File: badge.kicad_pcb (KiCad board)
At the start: 2 copper layers, 76.2 x 127 mm, 29 parts, among them J1 TC2030, SW1 SW_Push, SW2 SW_Push, SW3 SW_Push, SW4 SW_Push, SW5 SW_Push, U1 NHD-C12832A1Z-FSRGB-FBW-3V

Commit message: Add graffiti
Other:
- board text added: "Designed by SplitPixl, Assembled by you!"
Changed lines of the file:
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@@
 			(at 3.25 -2 0)
 			(layer "F.SilkS")
+			(hide yes)
 			(effects
 				(font
@@
 			(at 3.25 -2 0)
 			(layer "F.SilkS")
+			(hide yes)
 			(effects
 				(font
@@
 			(at 3.25 -2 0)
 			(layer "F.SilkS")
+			(hide yes)
 			(effects
 				(font
@@
 			(at 3.25 -2 0)
 			(layer "F.SilkS")
+			(hide yes)
 			(effects
 				(font
@@
 			(at 3.25 -2 0)
 			(layer "F.SilkS")
+			(hide yes)
 			(effects
 				(font
@@
 		)
 	)
+	(gr_text "Designed by SplitPixl,\nAssembled by you!"
+		(at 63.5 151.327 0)
+		(layer "B.SilkS")
+		(effects
+			(font
+				(size 1 1)
+				(thickness 0.1)
+			)
+			(justify bottom mirror)
+		)
+	)

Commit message: board can be turned off
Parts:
- added SW6: SW_SPST, FTbadge:SW_SLW-1277744-3A-N-D, F.Cu at (92.1, 42.1)
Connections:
- D1 pad 2: Net-(BT1-+) -> Net-(D1-A)
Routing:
- net Net-(D1-A): track 0.00 -> 54.7 mm
- net Net-(BT1-+): track 11.0 -> 39.3 mm

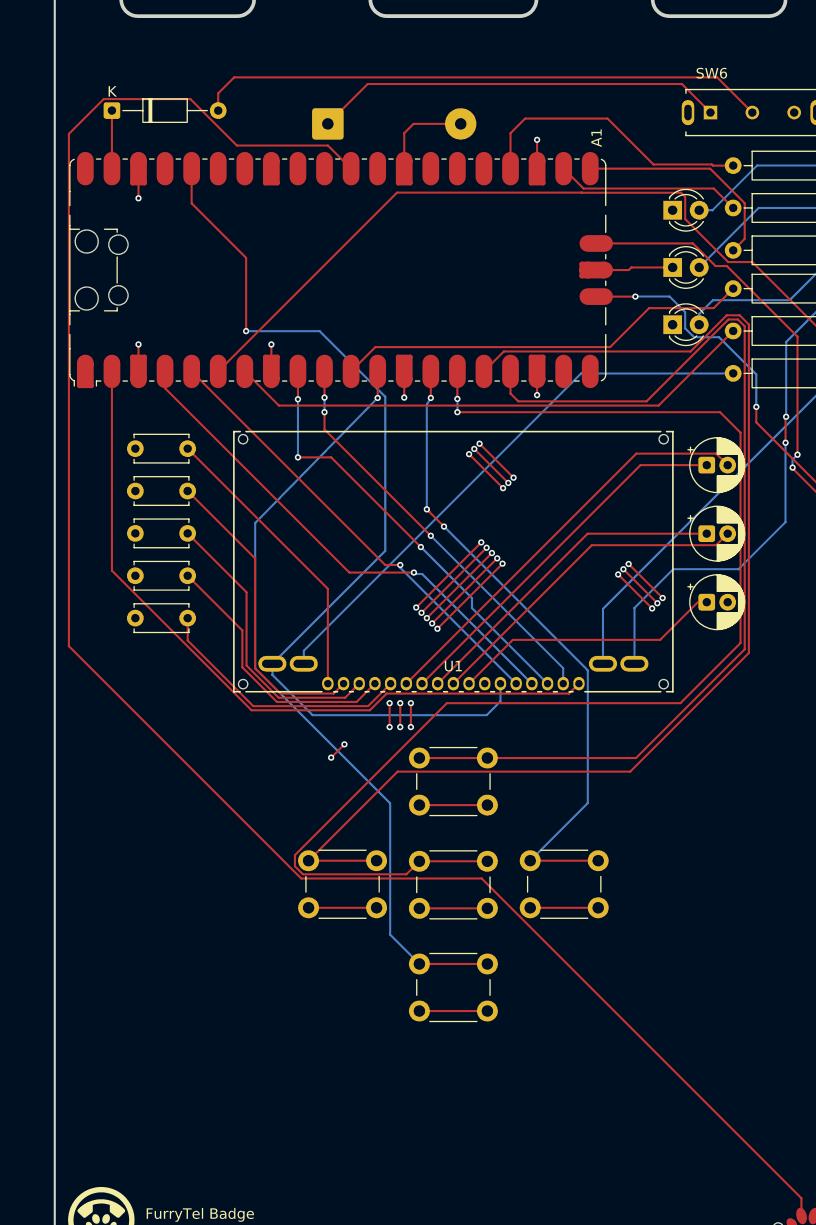
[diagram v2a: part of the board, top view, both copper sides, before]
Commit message: Add SAO connector
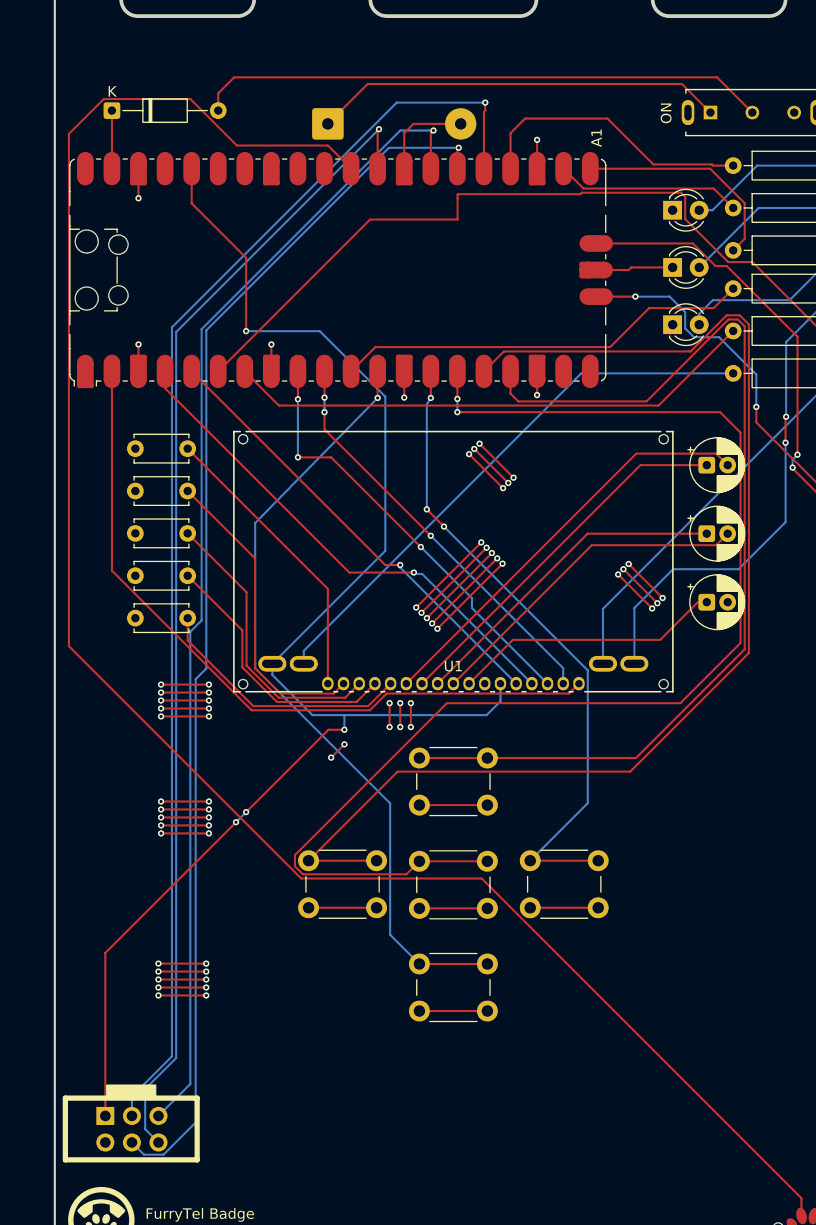
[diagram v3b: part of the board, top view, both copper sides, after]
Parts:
- added X1: Simple_Addon_v2, FTbadge:Simple_Addon_v2-BADGE-2x3, F.Cu at (32.7, 139.3)
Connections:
- A1 pad 25: unconnected-(A1-GPIO19-Pad25) -> Net-(A1-GPIO19)
- A1 pad 26: unconnected-(A1-GPIO20-Pad26) -> Net-(A1-GPIO20)
- A1 pad 27: unconnected-(A1-GPIO21-Pad27) -> Net-(A1-GPIO21)
- A1 pad 29: unconnected-(A1-GPIO22-Pad29) -> Net-(A1-GPIO22)
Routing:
- net Net-(A1-GPIO19): track 0.00 -> 122.2 mm, vias 0 -> 1
- net Net-(A1-GPIO20): track 0.00 -> 117.4 mm, vias 0 -> 1
- net Net-(A1-GPIO21): track 0.00 -> 110.7 mm, vias 0 -> 1
- net Net-(A1-GPIO22): track 0.00 -> 110.5 mm, vias 0 -> 1
- net (no net): track 0.00 -> 68.6 mm, vias 0 -> 30
- net +3V3: track 90.3 -> 138.9 mm, vias 1 -> 4
- net Net-(A1-GPIO4): track 76.2 -> 77.6 mm
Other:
- board text added: "ON"

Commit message: Add cat!
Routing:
- net GND: track 147.3 -> 215.9 mm, vias 37 -> 67
- net (no net): track 68.6 -> 0.00 mm, vias 30 -> 0

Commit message: mild cleanup
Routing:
- net Net-(A1-GPIO19): track 122.2 -> 125.8 mm
- net Net-(A1-GPIO21): track 110.7 -> 110.2 mm
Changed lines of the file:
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@@
 			(at 0 -5.5 0)
 			(layer "B.SilkS")
+			(hide yes)
 			(effects
 				(font
@@
 			(at 0 -8.509 0)
 			(layer "F.Fab")
+			(hide yes)
 			(effects
 				(font
@@
 	)
 	(segment
-		(start 63.881 47.46)
-		(end 63.881 45.593)
+		(start 63.881 45.593)
+		(end 63.881 47.46)
 		(width 0.2)
 		(layer "F.Cu")
@@
 	)
 	(segment
-		(start 63.881 45.593)
-		(end 64.008 45.466)
+		(start 62.23 44.704)
+		(end 62.992 44.704)
+		(width 0.2)
+		(layer "F.Cu")
+		(net "Net-(A1-GPIO20)")
+	)
+	(segment
+		(start 62.992 44.704)
+		(end 63.881 45.593)
 		(width 0.2)
 		(layer "F.Cu")
@@
 	)
 	(via
-		(at 64.008 45.466)
+		(at 62.23 44.704)
 		(size 0.6)
 		(drill 0.3)
@@
 	)
 	(segment
-		(start 39.883471 62.917215)
-		(end 39.883471 95.244529)
+		(start 33.9356 141.7083)
+		(end 32.772 140.5447)
 		(width 0.2)
 		(layer "B.Cu")
@@
 	)
 	(segment
-		(start 35.793979 141.7083)
-		(end 33.9356 141.7083)
+		(start 58.096686 44.704)
+		(end 39.883471 62.917215)
 		(width 0.2)
 		(layer "B.Cu")
@@
 	)
 	(segment
-		(start 39.883471 95.244529)
-		(end 38.862 96.266)
+		(start 35.793979 141.7083)
+		(end 33.9356 141.7083)
 		(width 0.2)
 		(layer "B.Cu")
@@
 	)
 	(segment
-		(start 38.862 96.266)
-		(end 38.862 138.640279)
+		(start 38.862 138.640279)
+		(end 35.793979 141.7083)
 		(width 0.2)
 		(layer "B.Cu")
@@
 	)
 	(segment
-		(start 57.334686 45.466)
-		(end 39.883471 62.917215)
+		(start 39.883471 95.244529)
+		(end 38.862 96.266)
 		(width 0.2)
 		(layer "B.Cu")
@@
 	)
 	(segment
-		(start 64.008 45.466)
-		(end 57.334686 45.466)
+		(start 38.862 96.266)
+		(end 38.862 138.640279)
 		(width 0.2)
 		(layer "B.Cu")
@@
 	)
 	(segment
-		(start 33.9356 141.7083)
-		(end 32.772 140.5447)
+		(start 39.883471 62.917215)
+		(end 39.883471 95.244529)
 		(width 0.2)
 		(layer "B.Cu")
@@
 	)
 	(segment
-		(start 38.862 138.640279)
-		(end 35.793979 141.7083)
+		(start 62.23 44.704)
+		(end 58.096686 44.704)
 		(width 0.2)
 		(layer "B.Cu")
@@
 	)
 	(segment
-		(start 61.595 43.815)
+		(start 60.198 43.815)
+		(end 61.087 43.815)
+		(width 0.2)
+		(layer "F.Cu")
+		(net "Net-(A1-GPIO21)")
+	)
+	(segment
+		(start 61.087 43.815)
 		(end 61.341 44.069)
 		(width 0.2)
@@
 	)
 	(via
-		(at 61.595 43.815)
+		(at 60.198 43.815)
 		(size 0.6)
 		(drill 0.3)
@@
 	)
 	(segment
-		(start 39.4335 90.646135)
-		(end 39.4335 62.8015)
+		(start 39.4335 62.8015)
+		(end 39.4335 90.646135)
 		(width 0.2)
 		(layer "B.Cu")
@@
 	)
 	(segment
-		(start 38.354 91.725635)
-		(end 39.4335 90.646135)
+		(start 38.354 134.9627)
+		(end 35.312 138.0047)
 		(width 0.2)
 		(layer "B.Cu")
@@
 	)
 	(segment
-		(start 35.312 138.0047)
+		(start 38.354 91.725635)
 		(end 38.354 134.9627)
 		(width 0.2)
@@
 	)
 	(segment
-		(start 39.4335 62.8015)
+		(start 60.198 43.815)
 		(end 58.42 43.815)
 		(width 0.2)
@@
 	)
 	(segment
-		(start 38.354 134.9627)
-		(end 38.354 91.725635)
+		(start 58.42 43.815)
+		(end 39.4335 62.8015)
 		(width 0.2)
 		(layer "B.Cu")
@@
 	)
 	(segment
-		(start 58.42 43.815)
-		(end 61.595 43.815)
+		(start 39.4335 90.646135)
+		(end 38.354 91.725635)
 		(width 0.2)
 		(layer "B.Cu")
@@
 	)
 	(segment
-		(start 66.421 42.037)
-		(end 66.421 47.46)
+		(start 68.072 40.132)
+		(end 66.421 41.783)
 		(width 0.2)
 		(layer "F.Cu")
@@
 	)
 	(segment
-		(start 66.548 41.91)
-		(end 66.421 42.037)
-		(width 0.2)
-		(layer "F.Cu")
-		(net "Net-(A1-GPIO19)")
-	)
-	(segment
-		(start 66.548 41.148)
-		(end 66.548 41.91)
+		(start 66.421 41.783)
+		(end 66.421 47.46)
 		(width 0.2)
 		(layer "F.Cu")
@@
 	)
 	(via
-		(at 66.548 41.148)
+		(at 68.072 40.132)
 		(size 0.6)
 		(drill 0.3)
@@
 	)
 	(segment
-		(start 36.6 132.31)
-		(end 32.766 136.144)
+		(start 36.6 62.627471)
+		(end 36.6 132.31)
 		(width 0.2)
 		(layer "B.Cu")
@@
 	)
 	(segment
-		(start 36.6 62.627471)
-		(end 36.6 132.31)
+		(start 36.6 132.31)
+		(end 32.766 136.144)
 		(width 0.2)
 		(layer "B.Cu")
@@
 	)
 	(segment
-		(start 58.079471 41.148)
-		(end 36.6 62.627471)
+		(start 32.766 136.144)
+		(end 32.772 136.15)
 		(width 0.2)
 		(layer "B.Cu")
@@
 	)
 	(segment
-		(start 32.772 136.15)
-		(end 32.772 138.0047)
+		(start 68.072 40.132)
+		(end 59.095471 40.132)
 		(width 0.2)
 		(layer "B.Cu")
@@
 	)
 	(segment
-		(start 32.766 136.144)
-		(end 32.772 136.15)
+		(start 59.095471 40.132)
+		(end 36.6 62.627471)
 		(width 0.2)
 		(layer "B.Cu")
@@
 	)
 	(segment
-		(start 66.548 41.148)
-		(end 58.079471 41.148)
+		(start 32.772 136.15)
+		(end 32.772 138.0047)
 		(width 0.2)
 		(layer "B.Cu")

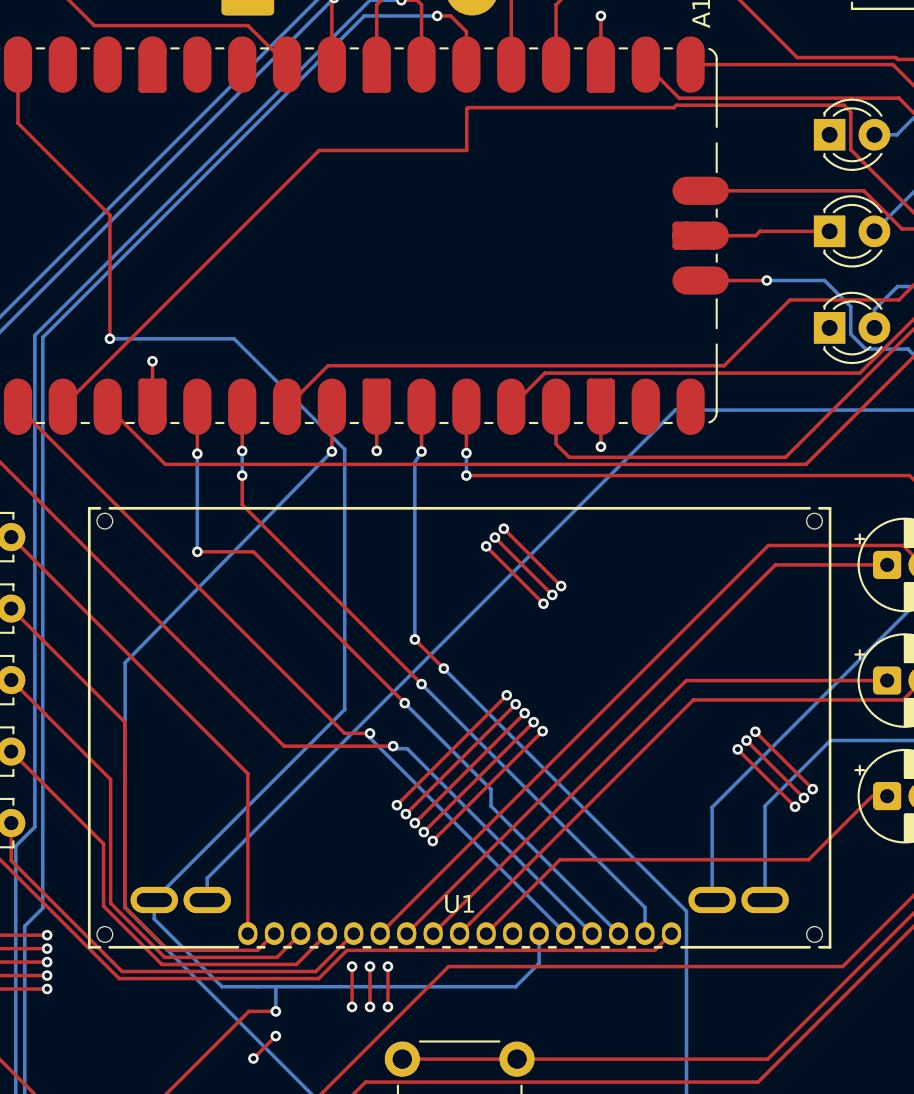
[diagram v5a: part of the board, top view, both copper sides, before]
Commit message: swap A0 and the green LED
this way the backlight colors are all on channel A of different PWM
peripherals.
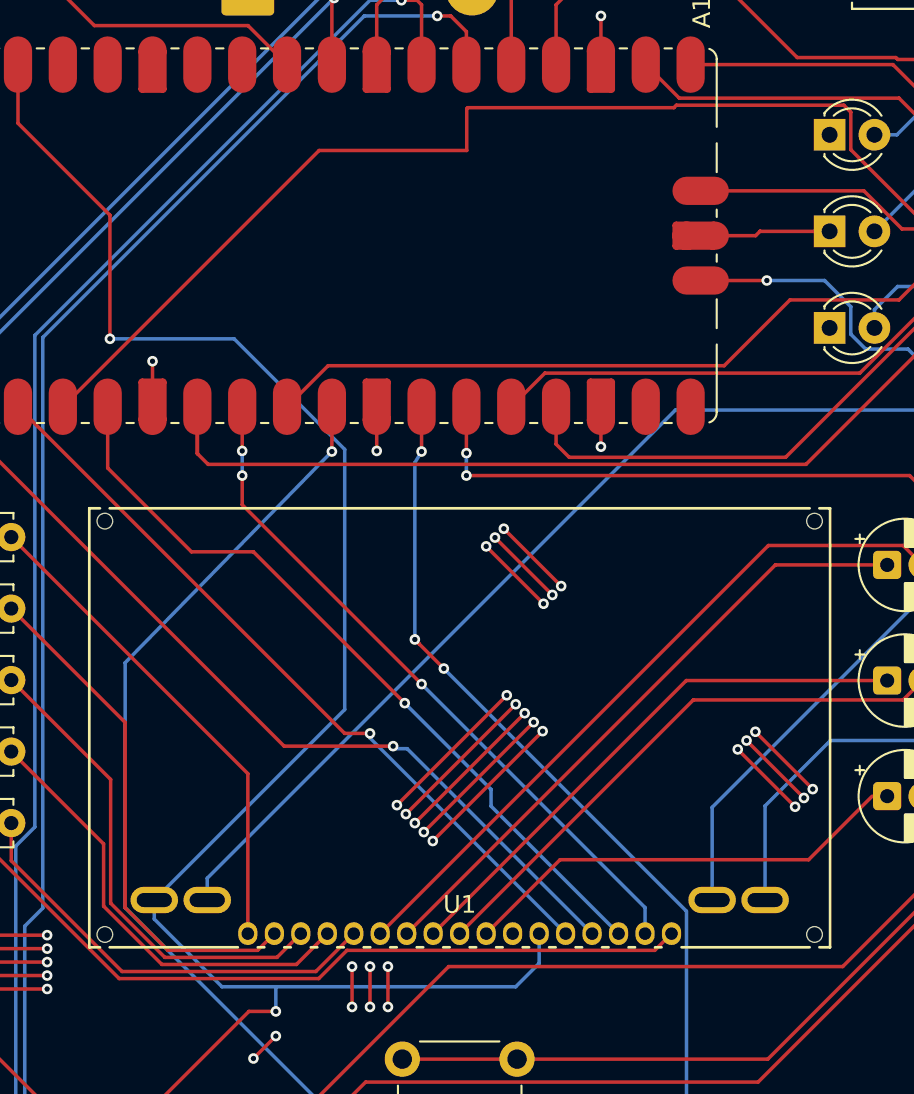
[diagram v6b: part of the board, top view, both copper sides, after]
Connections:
- A1 pad 7: Net-(A1-GPIO5) -> /A0
- A1 pad 9: /A0 -> Net-(A1-GPIO6)
- R2 pad 1: Net-(A1-GPIO5) -> Net-(A1-GPIO6)
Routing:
- net Net-(A1-GPIO5): track 51.0 -> 0.00 mm
- net Net-(A1-GPIO6): track 0.00 -> 50.1 mm
- net /A0: track 41.6 -> 43.9 mm, vias 3 -> 1
